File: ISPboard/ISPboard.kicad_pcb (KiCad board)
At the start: 2 copper layers, 80 x 50 mm, 17 parts, among them IC1 ATMEGA328-P, P1 5V, P2 ISP, P3 PB, P4 PC, P5 PD, P6 LED OUT, P7 BUTTON OUT, SW1 PUSH 1, SW2 PUSH 2

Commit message: Added the avr alarm project
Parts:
- added C1: 0.33uF, Capacitors_ThroughHole:C_Radial_D10_L20_P5, F.Cu at (110.3, 119.8)
- added C2: 0.1uF, Capacitors_ThroughHole:C_Radial_D10_L20_P7.5, F.Cu at (130.3, 108.8)
- added R4: 10k, Resistors_ThroughHole:Resistor_Vertical_RM5mm, F.Cu at (169.3, 116.3)
- added R5: 10k, Resistors_ThroughHole:Resistor_Vertical_RM5mm, F.Cu at (164.3, 116.3)
- added U1: LM7805CT, TO_SOT_Packages_THT:TO-220_Neutral123_Horizontal, F.Cu at (120.3, 112.8)
- P1: value 5V -> CONN_01X02
- moved SW1 28.0 mm to (181.3, 124.3)
- moved SW2 28.0 mm to (181.3, 114.3)
- moved D2 19.0 mm to (179.3, 103.1)
- moved D3 19.0 mm to (179.3, 96.1)
- moved D4 19.0 mm to (169.8, 132.3)
- moved IC1 19.0 mm to (141.5, 93.5)
- moved P2 19.0 mm to (147.3, 133.3)
- moved P4 19.0 mm to (156.8, 103.8)
- moved P6 19.0 mm to (156.8, 95.8)
- moved P7 19.0 mm to (156.8, 113.8)
- moved R1 19.0 mm to (168.1, 103.3)
- moved R2 19.0 mm to (168.6, 96.3)
- moved R3 19.0 mm to (161.8, 129.8)
- moved P3 19.0 mm to (133.3, 124.8)
- moved P5 19.0 mm to (133.3, 103.6)
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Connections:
- D1 pad 1: VCC -> Net-(C1-Pad1)
- D1 pad 2: Net-(D1-Pad2) -> VCC
- IC1 pad 20: VCC -> VDD
- IC1 pad 7: VCC -> VDD
- P1 pad 2: Net-(D1-Pad2) -> VCC
- P2 pad 2: VCC -> VDD
- R3 pad 2: VCC -> VDD
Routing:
- net VDD: track 0.00 -> 73.9 mm, vias 0 -> 2
- net VCC: track 48.1 -> 6.25 mm, vias 2 -> 0
- net Net-(C1-Pad1): track 0.00 -> 21.0 mm
- net Net-(P7-Pad2): track 13.0 -> 27.3 mm
- net Net-(P7-Pad1): track 10.1 -> 21.3 mm
- net Net-(D1-Pad2): track 8.80 -> 0.00 mm
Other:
- board text removed: "Andreas Fröderberg"
- board text removed: "ISP Programming board MK I"

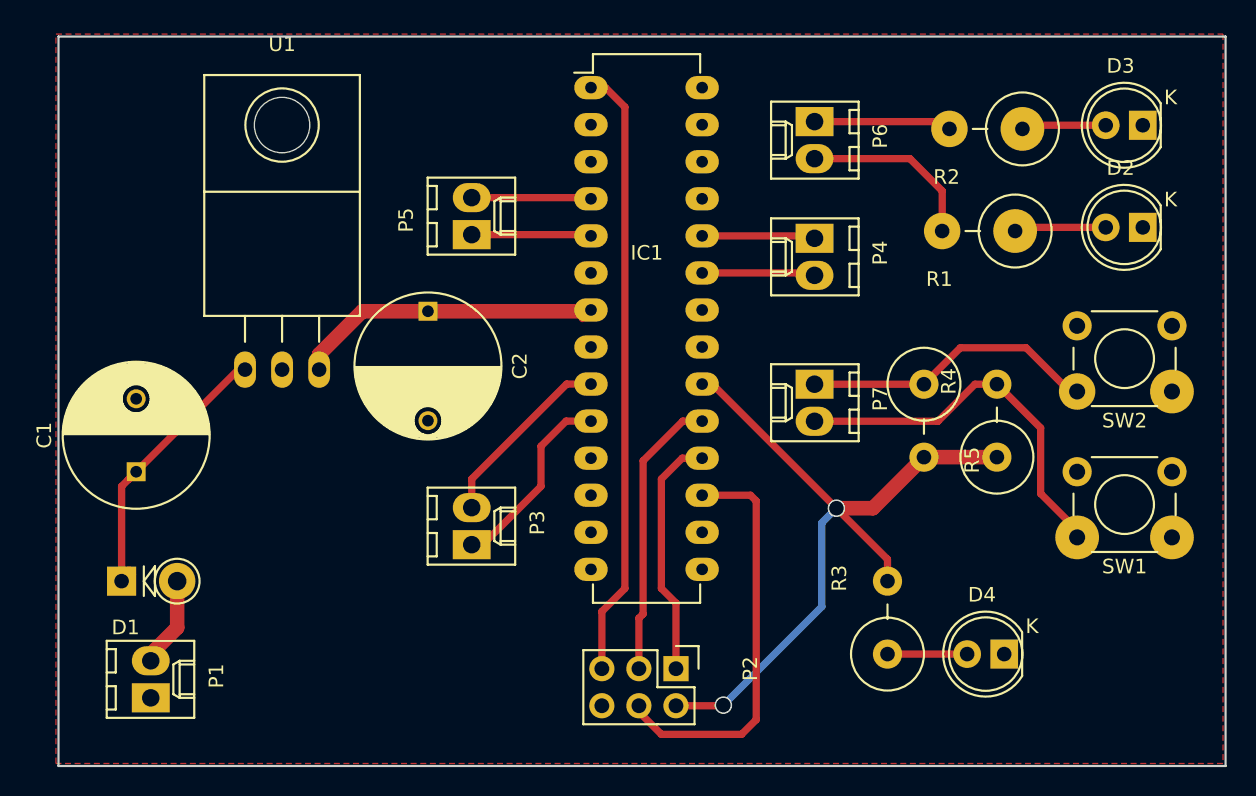
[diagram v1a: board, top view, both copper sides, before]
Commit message: Got display working on AVRAlarm
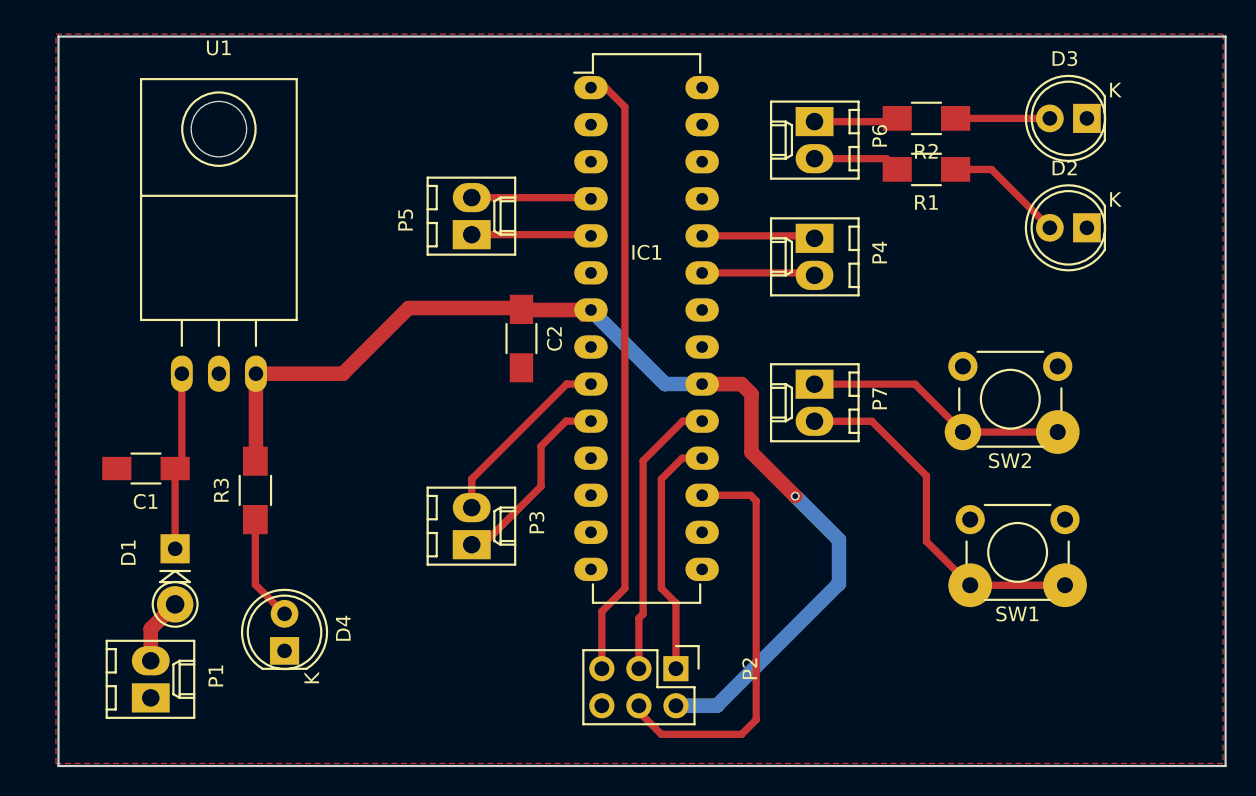
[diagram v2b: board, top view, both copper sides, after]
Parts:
- removed R4, R5: 10k, Resistors_ThroughHole:Resistor_Vertical_RM5mm
- C1: footprint Capacitors_ThroughHole:C_Radial_D10_L20_P5 -> Capacitors_SMD:C_1206_HandSoldering
- C2: footprint Capacitors_ThroughHole:C_Radial_D10_L20_P7.5 -> Capacitors_SMD:C_1206_HandSoldering
- R1, R2, R3: footprint Resistors_ThroughHole:Resistor_Vertical_RM5mm -> Resistors_SMD:R_1206_HandSoldering
- moved D4 49.3 mm to (120.5, 132.1), turned to 90 degrees
- moved R3 44.2 mm to (118.5, 121.1)
- moved SW2 8.31 mm to (173.5, 117.1)
- moved SW1 8.03 mm to (174.0, 127.6)
- moved C2 6.68 mm to (136.7, 110.7)
- moved R1 5.53 mm to (164.5, 99.1)
- moved U1 4.34 mm to (116.0, 113.1)
- moved D1 4.29 mm to (113.0, 125.1), turned to 270 degrees
- moved R2 4.14 mm to (164.5, 95.6)
- moved D3 3.86 mm to (175.5, 95.6)
- moved D2 3.83 mm to (175.5, 103.1)
- moved C1 0.71 mm to (111.0, 119.6), turned to 180 degrees
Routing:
- net Net-(C1-Pad1): track 21.0 -> 13.9 mm
- net Net-(P6-Pad2): track 12.4 -> 5.98 mm
- net Net-(P6-Pad1): track 10.2 -> 5.76 mm
- net Net-(D2-Pad2): track 6.31 -> 8.47 mm
- net Net-(P7-Pad2): track 27.3 -> 25.5 mm
- net Net-(D4-Pad2): track 5.46 -> 7.29 mm
- net Net-(P7-Pad1): track 21.3 -> 19.5 mm
- net VDD: track 73.9 -> 75.4 mm, vias 2 -> 3
- net VCC: track 6.25 -> 5.07 mm
- net Net-(D3-Pad2): track 5.81 -> 6.81 mm

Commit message: Fine tuned ispboard v2.
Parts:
- removed D1: D_Schottky, Diodes_ThroughHole:Diode_DO-41_SOD81_Vertical_KathodeUp
- removed U1: LM7805CT, TO_SOT_Packages_THT:TO-220_Neutral123_Horizontal
- added C3: 22uF, Capacitors_SMD:c_elec_4x4.5, F.Cu at (128.0, 102.1)
- added CBOOT1: 10nF, Capacitors_SMD:C_0805_HandSoldering, F.Cu at (122.5, 119.1)
- added CIN1: 10uF, Capacitors_SMD:c_elec_4x4.5, F.Cu at (118.5, 124.5)
- added Css1: 0.1uF, Capacitors_SMD:C_0805_HandSoldering, F.Cu at (113.5, 123.5)
- added L1: 15uH, Choke_SMD:Choke_SMD_Wuerth-WE-PD2-Typ-L, F.Cu at (125.5, 111.5)
- added P8: CONN_01X02, Connectors_Molex:Molex_KK-6410-02_02x2.54mm_Straight, B.Cu at (139.0, 95.0)
- added R4: 45.3k, Resistors_SMD:R_1206_HandSoldering, F.Cu at (117.5, 109.5)
- added R5: 100k, Resistors_SMD:R_1206_HandSoldering, F.Cu at (110.5, 123.5)
- added R6: 10k, Resistors_SMD:R_1206_HandSoldering, F.Cu at (117.5, 113.5)
- added REG1: RT8284, Power_Integrations:SO-8, F.Cu at (117.5, 118.5)
- added Rc1: 13k, Resistors_SMD:R_1206_HandSoldering, F.Cu at (110.5, 110.5)
- C1: value 0.33uF -> 3.3nF; footprint Capacitors_SMD:C_1206_HandSoldering -> Capacitors_SMD:C_0805_HandSoldering
- C2: value 0.1uF -> 22uF; footprint Capacitors_SMD:C_1206_HandSoldering -> Capacitors_SMD:c_elec_4x4.5
- D2, D3, D4, IC1, P3, P4, P5, P6, P7, SW1, SW2: moved to B.Cu
- P1: footprint Connectors_Molex:Molex_KK-6410-02_02x2.54mm_Straight -> Socket_Strips:Socket_Strip_Straight_1x02
- P2: footprint Pin_Headers:Pin_Header_Straight_2x03 -> Socket_Strips:Socket_Strip_Straight_2x03
- moved D3 50.2 mm to (142.5, 133.5), turned to 90 degrees
- moved P3 38.7 mm to (158.0, 95.0), turned to 180 degrees
- moved D4 38.6 mm to (117.5, 93.6), turned to 270 degrees
- moved D2 38.1 mm to (152.5, 133.5), turned to 90 degrees
- moved P2 37.6 mm to (176.0, 109.0), turned to 90 degrees
- moved R2 33.5 mm to (146.0, 123.5), turned to 90 degrees
- moved P6 26.3 mm to (151.0, 121.5), turned to 0 degrees
- moved R1 25.1 mm to (158.5, 123.5), turned to 90 degrees
- moved P4 24.0 mm to (137.2, 117.6), turned to 0 degrees
- moved R3 19.9 mm to (112.5, 102.1), turned to 270 degrees
- moved C2 18.8 mm to (120.0, 102.1), turned to 90 degrees
- moved P5 17.8 mm to (149.0, 95.1), turned to 180 degrees
- moved P7 16.6 mm to (171.5, 121.5), turned to 180 degrees
- moved P1 15.6 mm to (124.5, 127.0)
- moved SW2 11.4 mm to (174.0, 128.5), turned to 270 degrees
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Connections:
- net /PB0 renamed /PB6
- net /PB1 renamed /PB7
- net /PD0 renamed /PD3
- net /PD1 renamed /PD2
- C1 pad 2: GND -> Net-(C1-Pad2)
- IC1 pad 2: (no net) -> /RX
- IC1 pad 3: (no net) -> /TX
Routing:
- net VDD: track 75.4 -> 98.8 mm, vias 3 -> 2
- net VCC: track 5.07 -> 27.8 mm
- net Net-(C1-Pad1): track 13.9 -> 2.75 mm
- net Net-(P7-Pad2): track 25.5 -> 14.7 mm
- net /TX: track 0.00 -> 8.27 mm
- net /RX: track 0.00 -> 8.15 mm
- net Net-(R4-Pad2): track 0.00 -> 7.42 mm
- net /PC0: track 7.78 -> 14.9 mm
- net /PB7: track 14.3 -> 7.65 mm
- net Net-(CBOOT1-Pad2): track 0.00 -> 6.45 mm
- net Net-(R5-Pad2): track 0.00 -> 6.36 mm
- net /PB6: track 12.8 -> 7.65 mm
- net Net-(P7-Pad1): track 19.5 -> 14.5 mm
- net /PC1: track 7.78 -> 12.8 mm
- net Net-(C1-Pad2): track 0.00 -> 4.25 mm
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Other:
- board text removed: "+"
- board text removed: "-"
- board text removed: "PB0"
- board text removed: "PB1"
- board text removed: "PC0"
- board text removed: "PC1"
- board text removed: "PD0"
- board text removed: "PD1"
